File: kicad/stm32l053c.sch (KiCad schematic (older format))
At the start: 47 parts, among them J1 Water_Level, J2 Motion, J3 Door, J4 Door_Led, J5 AIN3, J6 Pump, J7 BATTERY, P1 SWD, Q1 Q_NMOS_GSD, U1 MCP1703A-3302_SOT223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

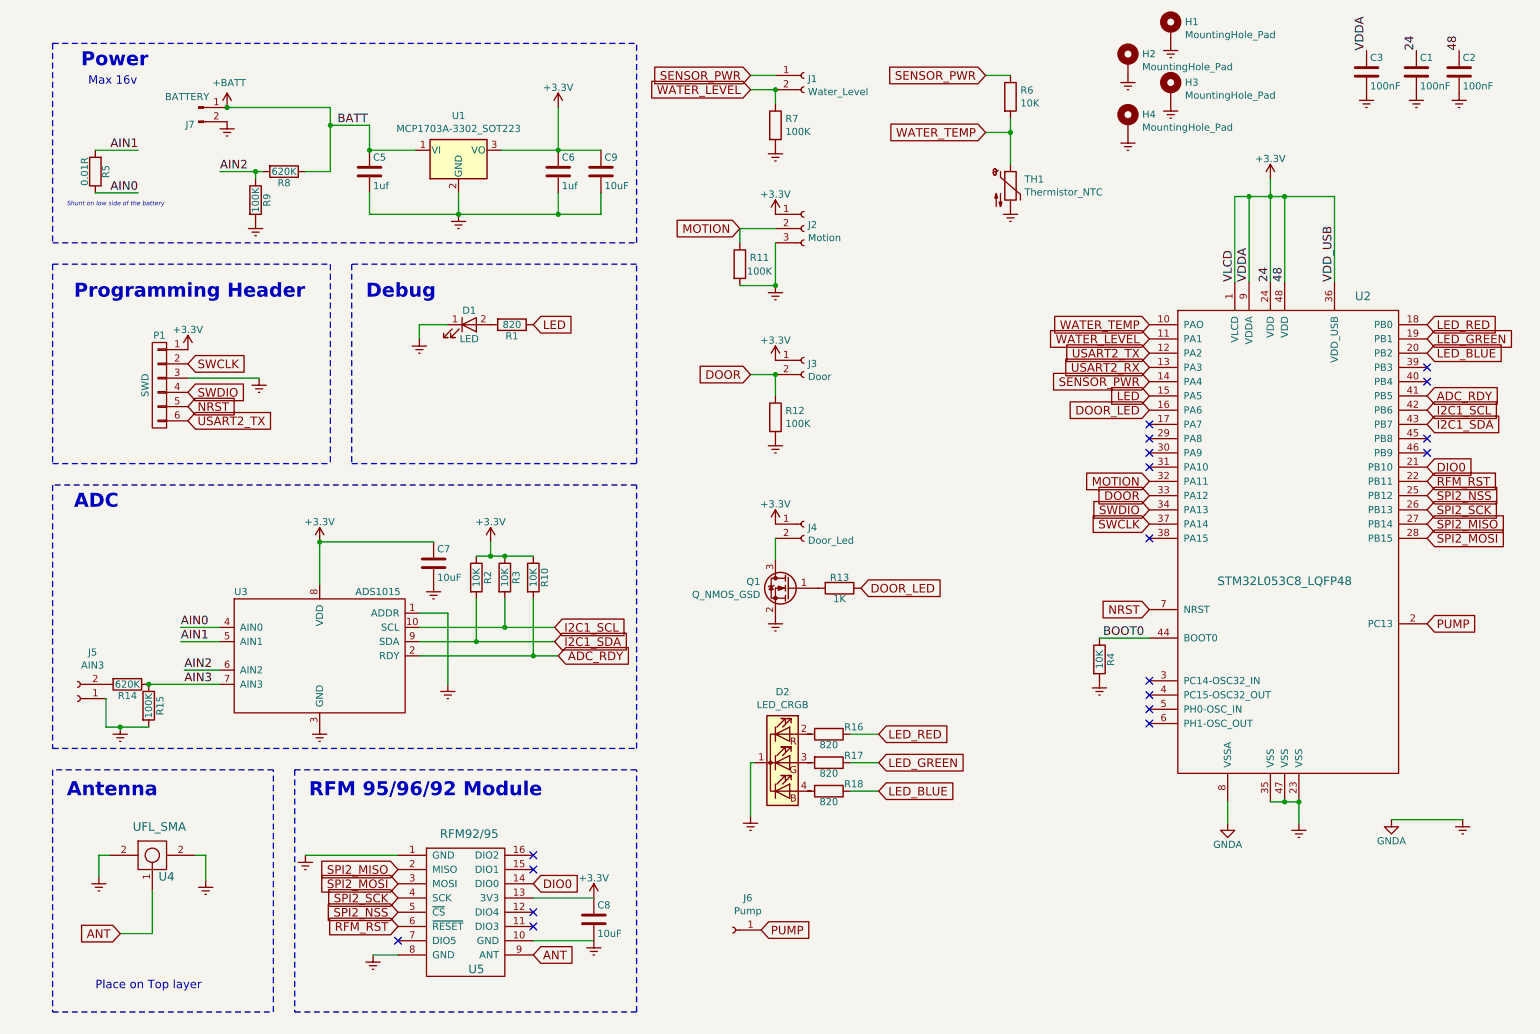
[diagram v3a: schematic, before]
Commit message: 5V regulator before the 3V3 one
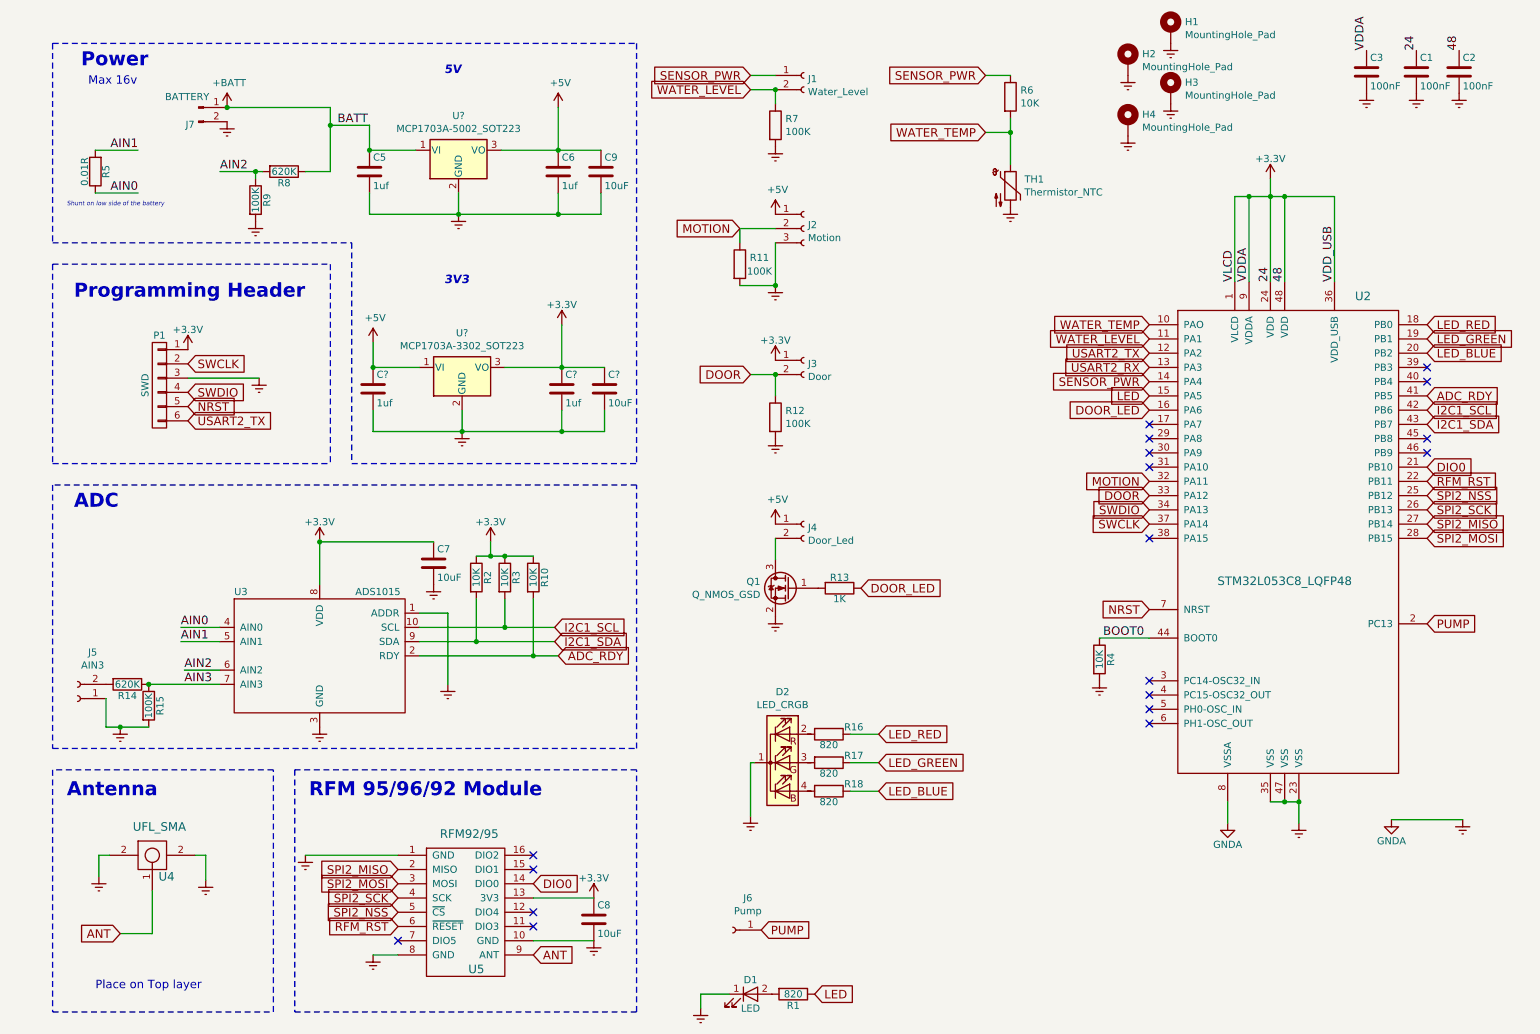
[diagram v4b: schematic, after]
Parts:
- removed U1: MCP1703A-3302_SOT223, Package_TO_SOT_SMD:SOT-223-3_TabPin2, symbol Regulator_Linear:MCP1703A-3302_SOT223
- added C? (x2): 1uf, Capacitors_SMD:C_0805_HandSoldering, symbol stm32l053c-rescue:C
- added C?: 10uF, Capacitors_SMD:C_0805_HandSoldering, symbol stm32l053c-rescue:C
- added U?: MCP1703A-3302_SOT223, Package_TO_SOT_SMD:SOT-223-3_TabPin2, symbol Regulator_Linear:MCP1703A-3302_SOT223
- added U?: MCP1703A-5002_SOT223, Package_TO_SOT_SMD:SOT-223-3_TabPin2, symbol Regulator_Linear:MCP1703A-5002_SOT223
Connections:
- net +3V3: now also C?.1, C?.1, U?.3 (VO); no longer C6.1, C9.1, J2.1 (Pin_1), J4.1 (Pin_1)
- net +BATT: now also U?.1 (VI)
- net Earth: now also C?.2, C?.2, C?.2, U?.2 (GND), U?.2 (GND)
- new net +5V: C6.1, C9.1, C?.1, J2.1 (Pin_1), J4.1 (Pin_1), U?.1 (VI), U?.3 (VO)
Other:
- note added: "3V3"
- note added: "5V"
- note removed: "Debug"
- moved on the sheet: D1, R1
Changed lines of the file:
@@
 L stm32l053c-rescue:R R1
 U 1 1 580770D7
-P 4200 2700
-F 0 "R1" V 4280 2700 50  0000 C CNN
-F 1 "820" V 4200 2700 50  0000 C CNN
-F 2 "Resistor_SMD:R_0805_2012Metric_Pad1.15x1.40mm_HandSolder" V 4130 2700 50  0001 C CNN
-F 3 "" H 4200 2700 50  0000 C CNN
-	1    4200 2700
+P 6175 7400
+F 0 "R1" V 6255 7400 50  0000 C CNN
+F 1 "820" V 6175 7400 50  0000 C CNN
+F 2 "Resistor_SMD:R_0805_2012Metric_Pad1.15x1.40mm_HandSolder" V 6105 7400 50  0001 C CNN
+F 3 "" H 6175 7400 50  0000 C CNN
+	1    6175 7400
 	0    1    1    0
 $EndComp
@@
 L power:Earth #PWR010
 U 1 1 58077163
-P 3550 2800
-F 0 "#PWR010" H 3550 2550 50  0001 C CNN
-F 1 "Earth" H 3550 2650 50  0001 C CNN
-F 2 "" H 3550 2800 50  0000 C CNN
-F 3 "" H 3550 2800 50  0000 C CNN
-	1    3550 2800
+P 5525 7500
+F 0 "#PWR010" H 5525 7250 50  0001 C CNN
+F 1 "Earth" H 5525 7350 50  0001 C CNN
+F 2 "" H 5525 7500 50  0000 C CNN
+F 3 "" H 5525 7500 50  0000 C CNN
+	1    5525 7500
 	-1   0    0    -1
 $EndComp
@@
 L stm32l053c-rescue:LED D1
 U 1 1 592DE199
-P 3900 2700
-F 0 "D1" H 3900 2800 50  0000 C CNN
-F 1 "LED" H 3900 2600 50  0000 C CNN
-F 2 "LEDs:LED_0805" H 3900 2700 50  0001 C CNN
-F 3 "" H 3900 2700 50  0001 C CNN
-	1    3900 2700
+P 5875 7400
+F 0 "D1" H 5875 7500 50  0000 C CNN
+F 1 "LED" H 5875 7300 50  0000 C CNN
+F 2 "LEDs:LED_0805" H 5875 7400 50  0001 C CNN
+F 3 "" H 5875 7400 50  0001 C CNN
+	1    5875 7400
 	1    0    0    -1
 $EndComp
@@
 RFM_RST
 $Comp
-L power:+3.3V #PWR013
-U 1 1 592F43A5
-P 4525 1175
-F 0 "#PWR013" H 4525 1025 50  0001 C CNN
-F 1 "+3.3V" H 4525 1315 50  0000 C CNN
-F 2 "" H 4525 1175 50  0001 C CNN
-F 3 "" H 4525 1175 50  0001 C CNN
-	1    4525 1175
-	1    0    0    -1
-$EndComp
-$Comp
 L power:+3.3V #PWR014
 U 1 1 592F4BC3
@@
 	1    0    0    -1
 $EndComp
-Text Notes 3175 2525 0    98   ~ 20
-Debug
 Text GLabel 10625 3800 2    60   Input ~ 0
 RFM_RST
@@
 Text GLabel 8675 3200 0    60   Input ~ 0
 LED
-Text GLabel 4350 2700 2    60   Input ~ 0
+Text GLabel 6325 7400 2    60   Input ~ 0
 LED
 Text GLabel 3400 6825 0    60   Input ~ 0
@@
 	10875 6175 10375 6175
 Wire Wire Line
-	3550 2800 3550 2700
-Wire Wire Line
-	3550 2700 3750 2700
+	5525 7500 5525 7400
+Wire Wire Line
+	5525 7400 5725 7400
 Wire Wire Line
 	9525 6050 9625 6050
@@
 Wire Wire Line
 	1675 6975 1450 6975
-Wire Notes Line
-	975  2125 5075 2125
 Wire Notes Line
 	975  725  5075 725
@@
 	4050 4325 4050 4225
 Wire Notes Line
-	3075 2275 3075 3675
-Wire Notes Line
 	3075 3675 5075 3675
-Wire Notes Line
-	5075 3675 5075 2275
-Wire Notes Line
-	5075 2275 3075 2275
 Wire Notes Line
 	975  725  975  2125
@@
 Text GLabel 8675 3000 0    60   Input ~ 0
 USART2_RX
-$Comp
-L Regulator_Linear:MCP1703A-3302_SOT223 U1
-U 1 1 5C23B6A9
-P 3825 1475
-F 0 "U1" H 3825 1717 50  0000 C CNN
-F 1 "MCP1703A-3302_SOT223" H 3825 1626 50  0000 C CNN
-F 2 "Package_TO_SOT_SMD:SOT-223-3_TabPin2" H 3825 1675 50  0001 C CNN
-F 3 "http://ww1.microchip.com/downloads/en/DeviceDoc/20005122B.pdf" H 3825 1425 50  0001 C CNN
-	1    3825 1475
-	1    0    0    -1
-$EndComp
 Wire Wire Line
 	3825 1775 3825 1925
@@
 Wire Wire Line
 	4125 1475 4525 1475
-Wire Notes Line
-	5075 2125 5075 725
 Connection ~ 9725 6050
 $Comp
@@
 F 3 "~" H 6250 2025 50  0001 C CNN
 	1    6250 2025
-	1    0    0    -1
-$EndComp
-$Comp
-L power:+3.3V #PWR027
-U 1 1 5C25C322
-P 6050 1925
-F 0 "#PWR027" H 6050 1775 50  0001 C CNN
-F 1 "+3.3V" H 6050 2065 50  0000 C CNN
-F 2 "" H 6050 1925 50  0001 C CNN
-F 3 "" H 6050 1925 50  0001 C CNN
-	1    6050 1925
 	1    0    0    -1
 $EndComp
@@
 	1    6050 4750
 	-1   0    0    -1
-$EndComp
-$Comp
-L power:+3.3V #PWR034
-U 1 1 5C28CF9B
-P 6050 4100
-F 0 "#PWR034" H 6050 3950 50  0001 C CNN
-F 1 "+3.3V" H 6050 4240 50  0000 C CNN
-F 2 "" H 6050 4100 50  0001 C CNN
-F 3 "" H 6050 4100 50  0001 C CNN
-	1    6050 4100
-	1    0    0    -1
 $EndComp
 $Comp
@@
 	2750 1625 2925 1625
 Wire Wire Line
-	2925 1625 2925 1300
-Wire Wire Line
 	2925 1300 3200 1300
 Wire Wire Line
@@
 Wire Wire Line
 	2200 1175 2925 1175
-Wire Wire Line
-	2925 1175 2925 1300
 Connection ~ 2200 1175
-Connection ~ 2925 1300
 $Comp
 L Mechanical:MountingHole_Pad H1
@@
 Text Notes 1075 1875 0    31   Italic 0
 Shunt on low side of the battery
+Connection ~ 2925 1300
+Wire Wire Line
+	2925 1175 2925 1300
+Wire Wire Line
+	2925 1625 2925 1300
+$Comp
+L power:Earth #PWR?
+U 1 1 5C254285
+P 3850 3450
+F 0 "#PWR?" H 3850 3200 50  0001 C CNN
+F 1 "Earth" H 3850 3300 50  0001 C CNN
+F 2 "" H 3850 3450 50  0000 C CNN
+F 3 "" H 3850 3450 50  0000 C CNN
+	1    3850 3450
+	1    0    0    -1
+$EndComp
+$Comp
+L power:+3.3V #PWR?
+U 1 1 5C25428B
+P 4550 2700
+F 0 "#PWR?" H 4550 2550 50  0001 C CNN
+F 1 "+3.3V" H 4550 2840 50  0000 C CNN
+F 2 "" H 4550 2700 50  0001 C CNN
+F 3 "" H 4550 2700 50  0001 C CNN
+	1    4550 2700
+	1    0    0    -1
+$EndComp
+$Comp
+L stm32l053c-rescue:C C?
+U 1 1 5C254291
+P 3225 3150
+F 0 "C?" H 3250 3250 50  0000 L CNN
+F 1 "1uf" H 3250 3050 50  0000 L CNN
+F 2 "Capacitors_SMD:C_0805_HandSoldering" H 3263 3000 50  0001 C CNN
+F 3 "" H 3225 3150 50  0001 C CNN
+	1    3225 3150
+	1    0    0    -1
+$EndComp
+$Comp
+L stm32l053c-rescue:C C?
+U 1 1 5C254298
+P 4550 3150
+F 0 "C?" H 4575 3250 50  0000 L CNN
+F 1 "1uf" H 4575 3050 50  0000 L CNN
+F 2 "Capacitors_SMD:C_0805_HandSoldering" H 4588 3000 50  0001 C CNN
+F 3 "" H 4550 3150 50  0001 C CNN
+	1    4550 3150
+	1    0    0    -1
+$EndComp
+Wire Wire Line
+	3225 3450 3850 3450
+Wire Wire Line
+	3225 3450 3225 3300
+Wire Wire Line
+	4550 3000 4550 2700
+Wire Wire Line
+	4550 3450 4550 3300
+Connection ~ 3850 3450
+$Comp
+L stm32l053c-rescue:C C?
+U 1 1 5C2542A4
+P 4850 3150
+F 0 "C?" H 4875 3250 50  0000 L CNN
+F 1 "10uF" H 4875 3050 50  0000 L CNN
+F 2 "Capacitors_SMD:C_0805_HandSoldering" H 4888 3000 50  0001 C CNN
+F 3 "" H 4850 3150 50  0000 C CNN
+	1    4850 3150
+	1    0    0    -1
+$EndComp
+Wire Wire Line
+	4850 3450 4850 3300
+Connection ~ 4550 3450
+Connection ~ 4550 3000
+Wire Wire Line
+	3850 3450 4550 3450
+Wire Wire Line
+	4550 3450 4850 3450
+Wire Wire Line
+	4550 3000 4850 3000
+$Comp
+L Regulator_Linear:MCP1703A-3302_SOT223 U?
+U 1 1 5C2542B2
+P 3850 3000
+F 0 "U?" H 3850 3242 50  0000 C CNN
+F 1 "MCP1703A-3302_SOT223" H 3850 3151 50  0000 C CNN
+F 2 "Package_TO_SOT_SMD:SOT-223-3_TabPin2" H 3850 3200 50  0001 C CNN
+F 3 "http://ww1.microchip.com/downloads/en/DeviceDoc/20005122B.pdf" H 3850 2950 50  0001 C CNN
+	1    3850 3000
+	1    0    0    -1
+$EndComp
+Wire Wire Line
+	3850 3300 3850 3450
+Wire Wire Line
+	3225 3000 3550 3000
+Wire Wire Line
+	4150 3000 4550 3000
+Wire Wire Line
+	3225 2825 3225 3000
+Connection ~ 3225 3000
+$Comp
+L Regulator_Linear:MCP1703A-5002_SOT223 U?
+U 1 1 5C257B3B
+P 3825 1475
+F 0 "U?" H 3825 1717 50  0000 C CNN
+F 1 "MCP1703A-5002_SOT223" H 3825 1626 50  0000 C CNN
+F 2 "Package_TO_SOT_SMD:SOT-223-3_TabPin2" H 3825 1675 50  0001 C CNN
+F 3 "http://ww1.microchip.com/downloads/en/DeviceDoc/20005122B.pdf" H 3825 1425 50  0001 C CNN
+	1    3825 1475
+	1    0    0    -1
+$EndComp
+$Comp
+L power:+5V #PWR?
+U 1 1 5C257EAB
+P 4525 1175
+F 0 "#PWR?" H 4525 1025 50  0001 C CNN
+F 1 "+5V" H 4540 1348 50  0000 C CNN
+F 2 "" H 4525 1175 50  0001 C CNN
+F 3 "" H 4525 1175 50  0001 C CNN
+	1    4525 1175
+	1    0    0    -1
+$EndComp
+$Comp
+L power:+5V #PWR?
+U 1 1 5C257F89
+P 3225 2825
+F 0 "#PWR?" H 3225 2675 50  0001 C CNN
+F 1 "+5V" H 3240 2998 50  0000 C CNN
+F 2 "" H 3225 2825 50  0001 C CNN
+F 3 "" H 3225 2825 50  0001 C CNN
+	1    3225 2825
+	1    0    0    -1
+$EndComp
+Text Notes 3725 2425 0    59   Italic 12
+3V3
+Text Notes 3725 950  0    59   Italic 12
+5V
+Wire Notes Line
+	975  2125 3075 2125
+Wire Notes Line
+	3075 2125 3075 3675
+Wire Notes Line
+	5075 725  5075 3675
+$Comp
+L power:+5V #PWR?
+U 1 1 5C25F4FD
+P 6050 1925
+F 0 "#PWR?" H 6050 1775 50  0001 C CNN
+F 1 "+5V" H 6065 2098 50  0000 C CNN
+F 2 "" H 6050 1925 50  0001 C CNN
+F 3 "" H 6050 1925 50  0001 C CNN
+	1    6050 1925
+	1    0    0    -1
+$EndComp
+$Comp
+L power:+5V #PWR?
+U 1 1 5C25FC69
+P 6050 4100
+F 0 "#PWR?" H 6050 3950 50  0001 C CNN
+F 1 "+5V" H 6065 4273 50  0000 C CNN
+F 2 "" H 6050 4100 50  0001 C CNN
+F 3 "" H 6050 4100 50  0001 C CNN
+	1    6050 4100
+	1    0    0    -1
+$EndComp
 $EndSCHEMATC

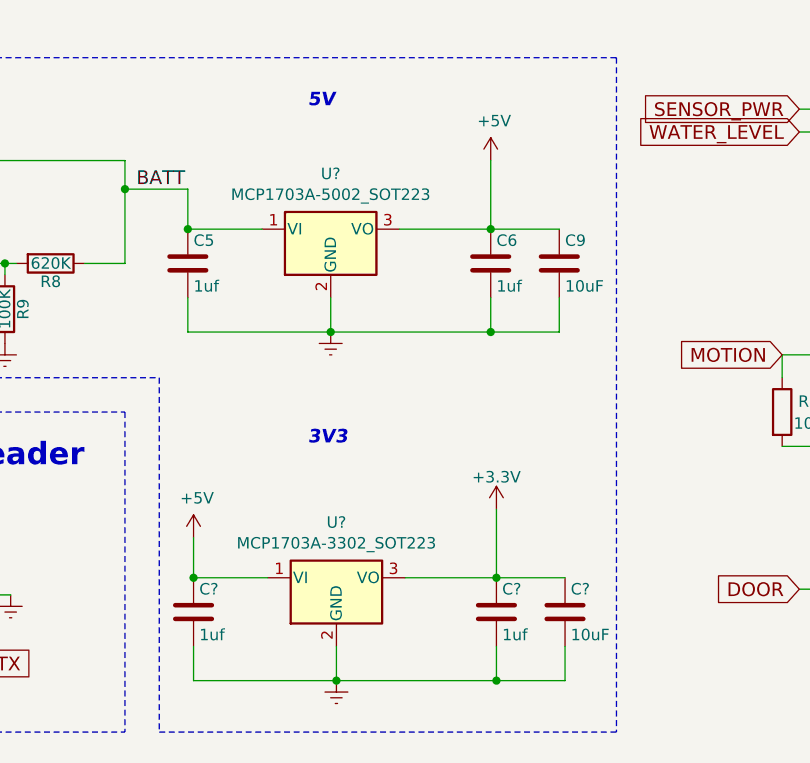
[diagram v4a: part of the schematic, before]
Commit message: 5V regulator before the 3V3 one
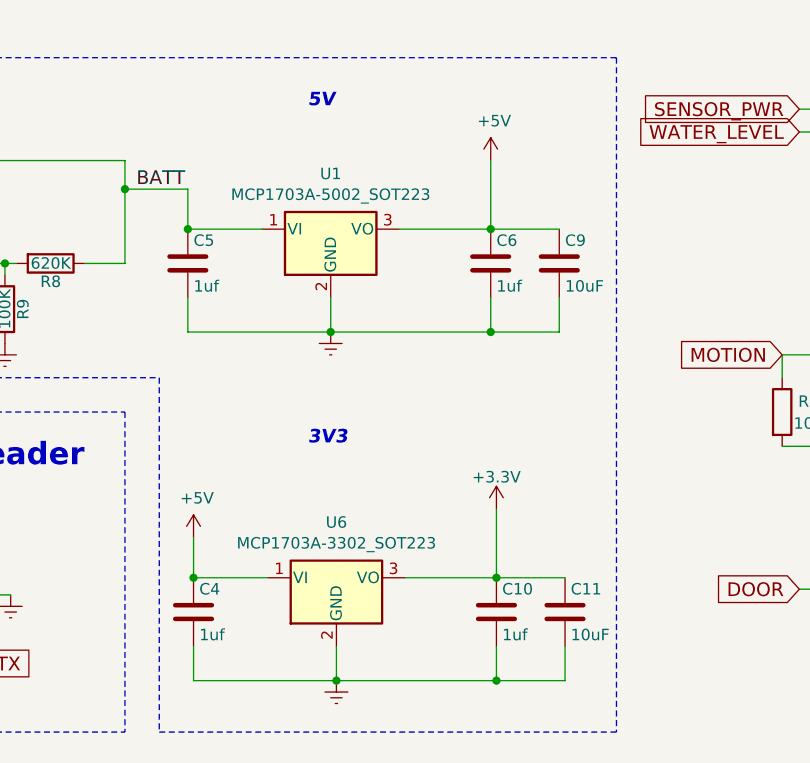
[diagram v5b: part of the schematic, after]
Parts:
- gave numbers to parts that had none: 5
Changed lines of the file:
@@
 	2925 1625 2925 1300
 $Comp
-L power:Earth #PWR?
+L power:Earth #PWR027
 U 1 1 5C254285
 P 3850 3450
-F 0 "#PWR?" H 3850 3200 50  0001 C CNN
+F 0 "#PWR027" H 3850 3200 50  0001 C CNN
 F 1 "Earth" H 3850 3300 50  0001 C CNN
 F 2 "" H 3850 3450 50  0000 C CNN
@@
 $EndComp
 $Comp
-L power:+3.3V #PWR?
+L power:+3.3V #PWR034
 U 1 1 5C25428B
 P 4550 2700
-F 0 "#PWR?" H 4550 2550 50  0001 C CNN
+F 0 "#PWR034" H 4550 2550 50  0001 C CNN
 F 1 "+3.3V" H 4550 2840 50  0000 C CNN
 F 2 "" H 4550 2700 50  0001 C CNN
@@
 $EndComp
 $Comp
-L stm32l053c-rescue:C C?
+L stm32l053c-rescue:C C4
 U 1 1 5C254291
 P 3225 3150
-F 0 "C?" H 3250 3250 50  0000 L CNN
+F 0 "C4" H 3250 3250 50  0000 L CNN
 F 1 "1uf" H 3250 3050 50  0000 L CNN
 F 2 "Capacitors_SMD:C_0805_HandSoldering" H 3263 3000 50  0001 C CNN
@@
 $EndComp
 $Comp
-L stm32l053c-rescue:C C?
+L stm32l053c-rescue:C C10
 U 1 1 5C254298
 P 4550 3150
-F 0 "C?" H 4575 3250 50  0000 L CNN
+F 0 "C10" H 4575 3250 50  0000 L CNN
 F 1 "1uf" H 4575 3050 50  0000 L CNN
 F 2 "Capacitors_SMD:C_0805_HandSoldering" H 4588 3000 50  0001 C CNN
@@
 Connection ~ 3850 3450
 $Comp
-L stm32l053c-rescue:C C?
+L stm32l053c-rescue:C C11
 U 1 1 5C2542A4
 P 4850 3150
-F 0 "C?" H 4875 3250 50  0000 L CNN
+F 0 "C11" H 4875 3250 50  0000 L CNN
 F 1 "10uF" H 4875 3050 50  0000 L CNN
 F 2 "Capacitors_SMD:C_0805_HandSoldering" H 4888 3000 50  0001 C CNN
@@
 	4550 3000 4850 3000
 $Comp
-L Regulator_Linear:MCP1703A-3302_SOT223 U?
+L Regulator_Linear:MCP1703A-3302_SOT223 U6
 U 1 1 5C2542B2
 P 3850 3000
-F 0 "U?" H 3850 3242 50  0000 C CNN
+F 0 "U6" H 3850 3242 50  0000 C CNN
 F 1 "MCP1703A-3302_SOT223" H 3850 3151 50  0000 C CNN
 F 2 "Package_TO_SOT_SMD:SOT-223-3_TabPin2" H 3850 3200 50  0001 C CNN
@@
 Connection ~ 3225 3000
 $Comp
-L Regulator_Linear:MCP1703A-5002_SOT223 U?
+L Regulator_Linear:MCP1703A-5002_SOT223 U1
 U 1 1 5C257B3B
 P 3825 1475
-F 0 "U?" H 3825 1717 50  0000 C CNN
+F 0 "U1" H 3825 1717 50  0000 C CNN
 F 1 "MCP1703A-5002_SOT223" H 3825 1626 50  0000 C CNN
 F 2 "Package_TO_SOT_SMD:SOT-223-3_TabPin2" H 3825 1675 50  0001 C CNN
@@
 $EndComp
 $Comp
-L power:+5V #PWR?
+L power:+5V #PWR028
 U 1 1 5C257EAB
 P 4525 1175
-F 0 "#PWR?" H 4525 1025 50  0001 C CNN
+F 0 "#PWR028" H 4525 1025 50  0001 C CNN
 F 1 "+5V" H 4540 1348 50  0000 C CNN
 F 2 "" H 4525 1175 50  0001 C CNN
@@
 $EndComp
 $Comp
-L power:+5V #PWR?
+L power:+5V #PWR013
 U 1 1 5C257F89
 P 3225 2825
-F 0 "#PWR?" H 3225 2675 50  0001 C CNN
+F 0 "#PWR013" H 3225 2675 50  0001 C CNN
 F 1 "+5V" H 3240 2998 50  0000 C CNN
 F 2 "" H 3225 2825 50  0001 C CNN
@@
 	5075 725  5075 3675
 $Comp
-L power:+5V #PWR?
+L power:+5V #PWR039
 U 1 1 5C25F4FD
 P 6050 1925
-F 0 "#PWR?" H 6050 1775 50  0001 C CNN
+F 0 "#PWR039" H 6050 1775 50  0001 C CNN
 F 1 "+5V" H 6065 2098 50  0000 C CNN
 F 2 "" H 6050 1925 50  0001 C CNN
@@
 $EndComp
 $Comp
-L power:+5V #PWR?
+L power:+5V #PWR044
 U 1 1 5C25FC69
 P 6050 4100
-F 0 "#PWR?" H 6050 3950 50  0001 C CNN
+F 0 "#PWR044" H 6050 3950 50  0001 C CNN
 F 1 "+5V" H 6065 4273 50  0000 C CNN
 F 2 "" H 6050 4100 50  0001 C CNN
